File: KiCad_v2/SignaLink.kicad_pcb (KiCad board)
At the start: 2 copper layers, 60.2 x 45 mm, 74 parts, among them U1 MT3608, U2 ESP32-C3_SUPERMINI_TH, U3 DM-OLED096-636, U4 MPU-6050, U5 BNO085, U6 MCP73871, U7 LTC4415IMSE_PBF, U8 TPS54331

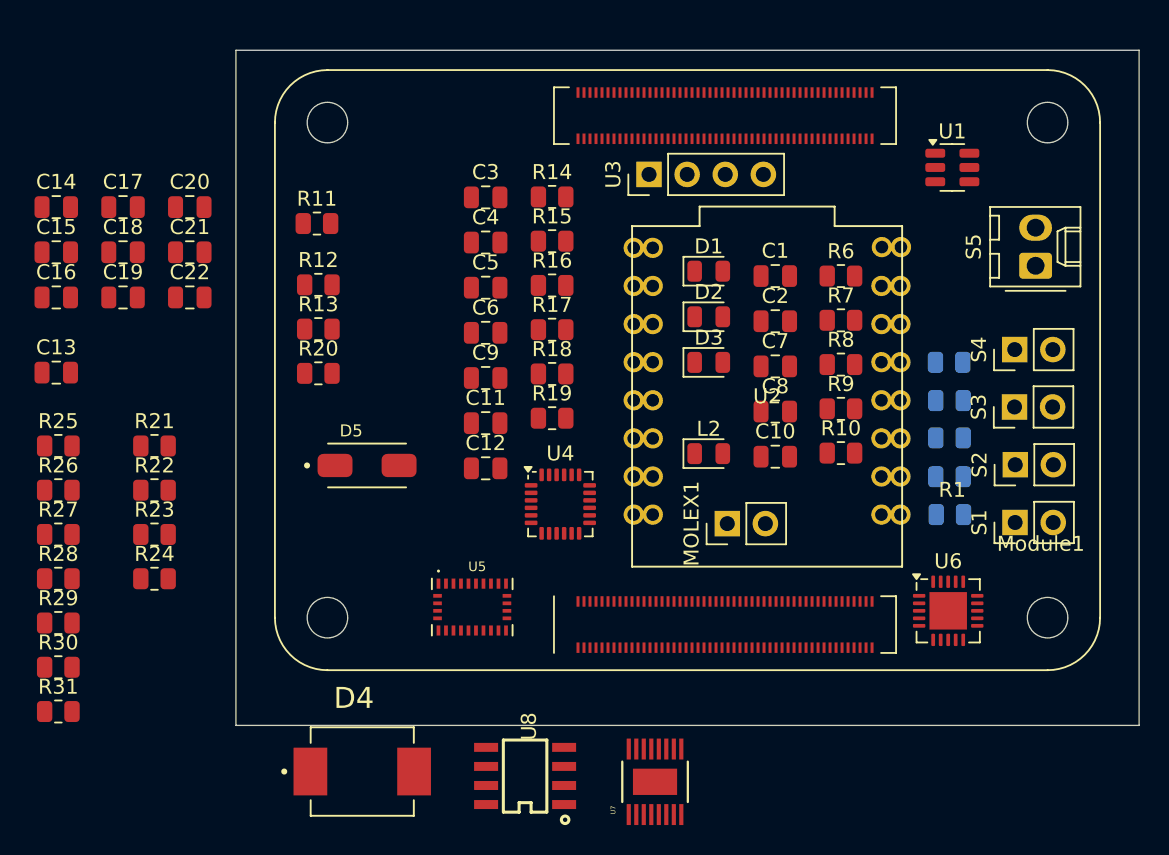
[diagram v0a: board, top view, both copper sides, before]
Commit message: feat: agrego 3d de ESP32 Y CM4
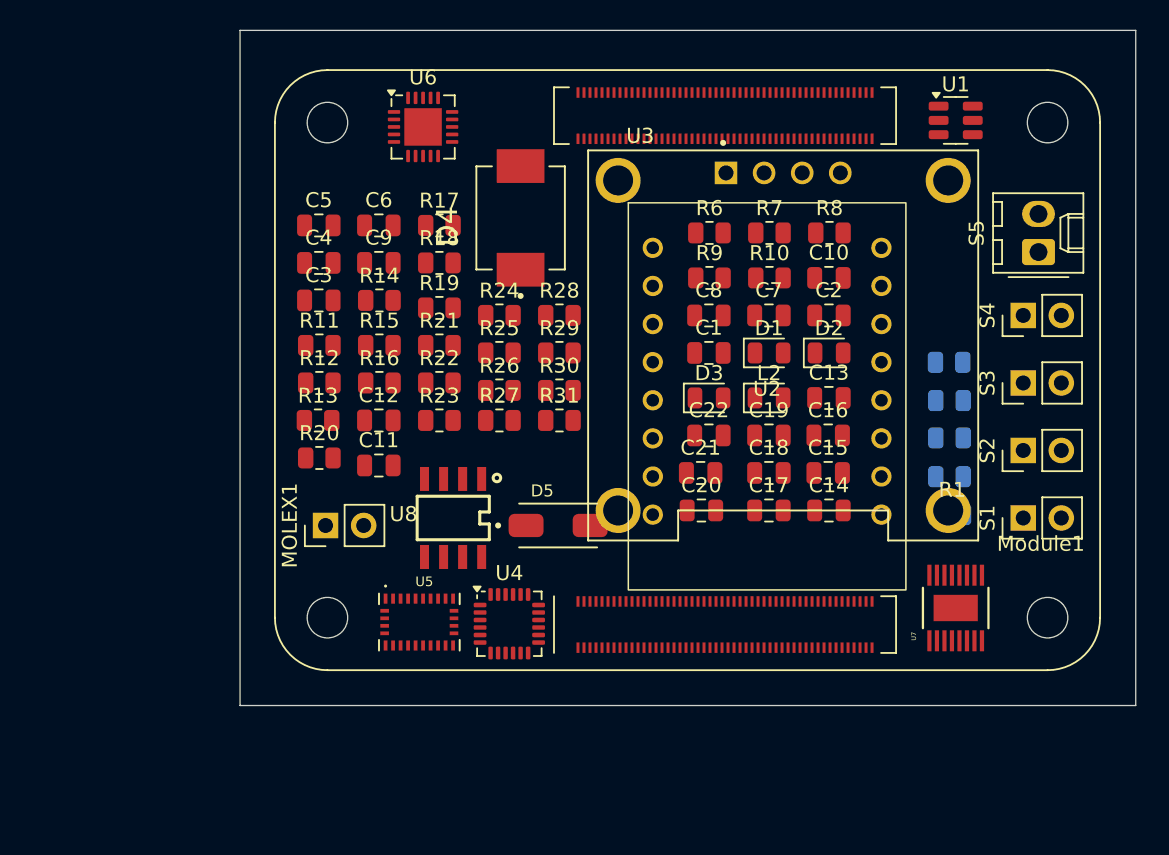
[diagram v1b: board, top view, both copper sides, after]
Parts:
- D4: footprint Footprint KiCad:DIOM7959X265N -> Custom_Footprints:DIOM7959X265N
- D5: footprint Footprint KiCad:B340A -> Custom_Footprints:B340A
- L2: value 22uH-4.7u -> 4.7uH
- U2: footprint esp32-huella:MODULE_ESP32-C3_SUPERMINI_TH -> Custom_Footprints:MODULE_ESP32-C3_SUPERMINI_TH
- U3: footprint Connector_PinHeader_2.54mm:PinHeader_1x04_P2.54mm_Vertical -> Custom_Footprints:MODULE_DM-OLED096-636
- U5: footprint Footprint KiCad:IC_BNO085 -> Custom_Footprints:IC_BNO085
- U7: footprint Footprint KiCad:MSOP-16_MSE -> Custom_Footprints:MSOP-16_MSE
- U8: footprint Footprint KiCad:SOP8 -> Custom_Footprints:SOP8
- moved C14 55.3 mm to (73.0, 79.0)
- moved C15 53.5 mm to (73.0, 76.5)
- moved C16 52.3 mm to (73.0, 74.0)
- moved C13 51.5 mm to (73.0, 71.5)
- moved U6 47.6 mm to (46.0, 53.4)
- moved C17 47.6 mm to (69.0, 79.0)
- moved C18 45.5 mm to (69.0, 76.5)
- moved C19 44.0 mm to (69.0, 74.0)
- moved C20 39.6 mm to (64.5, 79.0)
- moved R31 38.6 mm to (55.1, 73.0)
- moved D4 38.4 mm to (52.5, 59.5), turned to 90 degrees
- moved R30 38.2 mm to (55.1, 71.0)
- moved R29 37.9 mm to (55.1, 68.5)
- moved R28 37.7 mm to (55.1, 66.0)
- moved C21 37.1 mm to (64.5, 76.5)
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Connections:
- U2 pad 0: /A0 -> unconnected-(U2-GPIO0-Pad0)
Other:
- board size 60.2 x 45 mm -> 59.7 x 45 mm

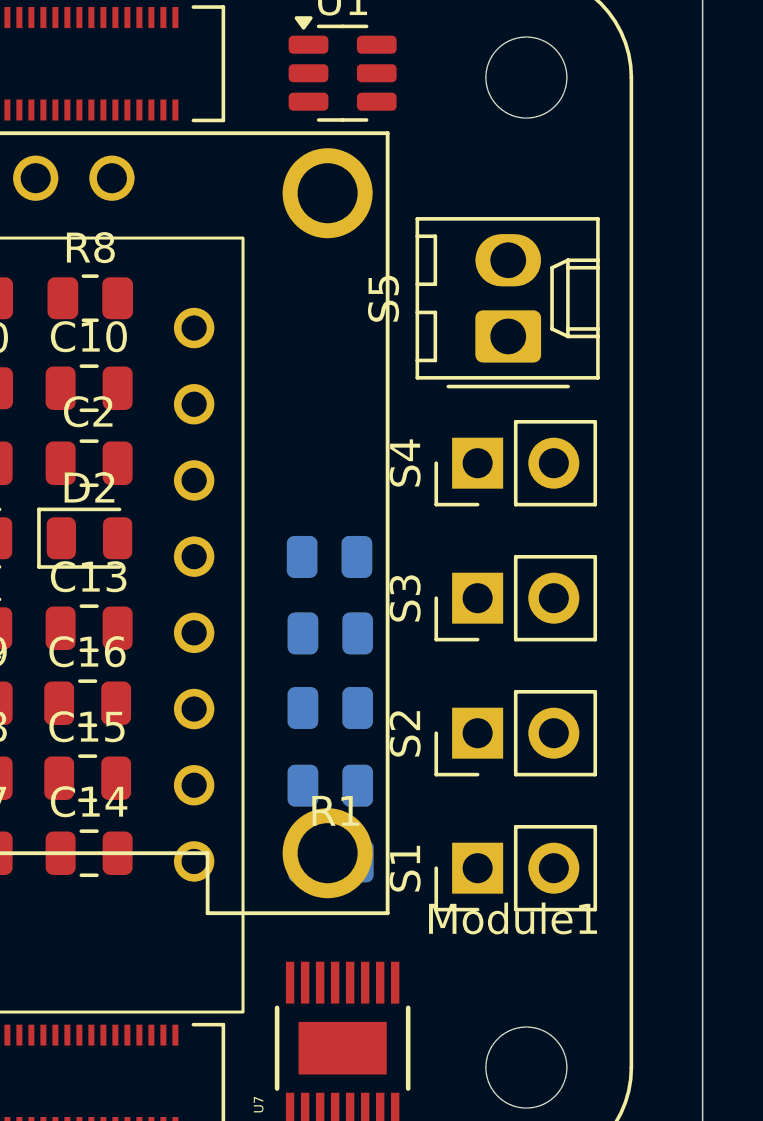
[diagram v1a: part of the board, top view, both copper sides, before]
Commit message: feat:footprint de molex en flex
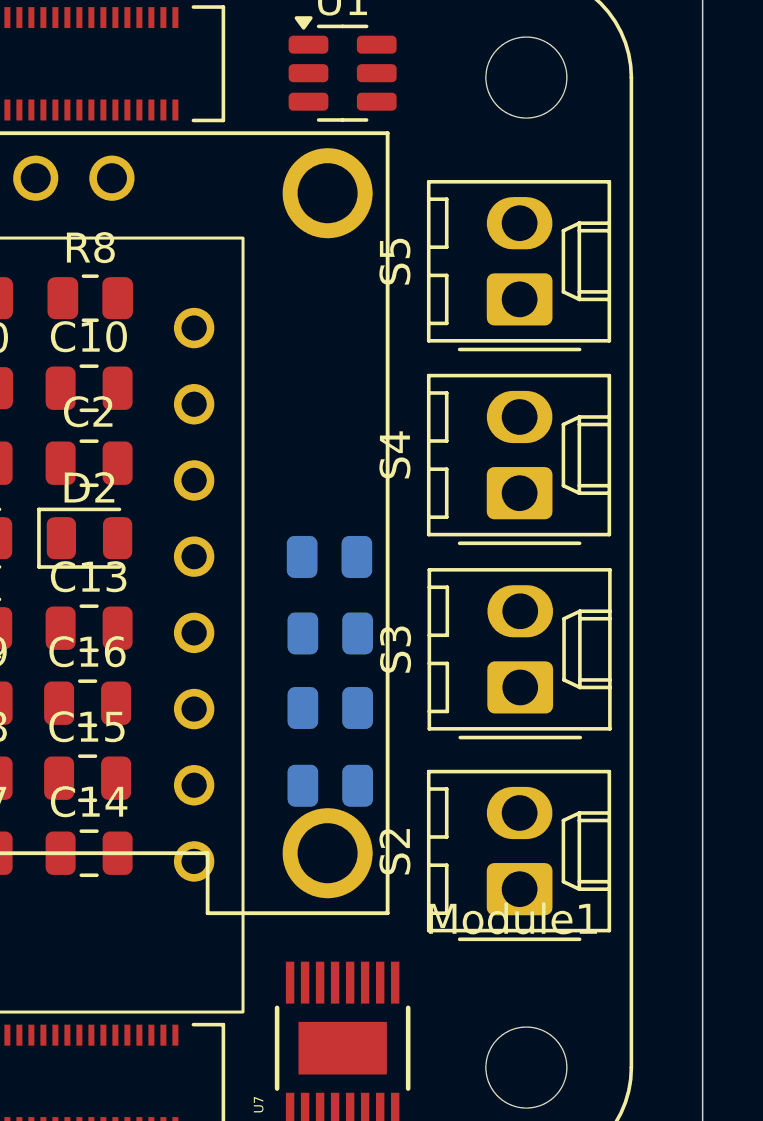
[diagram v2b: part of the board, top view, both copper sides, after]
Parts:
- removed R1: 10k, Resistor_SMD:R_0805_2012Metric
- removed S1: SF 1, Connector_PinHeader_2.54mm:PinHeader_1x02_P2.54mm_Vertical
- S2, S3, S4: footprint Connector_PinHeader_2.54mm:PinHeader_1x02_P2.54mm_Vertical -> Connector_Molex:Molex_KK-254_AE-6410-02A_1x02_P2.54mm_Vertical
- moved S2 5.39 mm to (87.4, 80.2)
- moved S3 3.30 mm to (87.4, 73.5)
- moved S4 1.72 mm to (87.4, 67.0)
- moved S5 1.29 mm to (87.4, 60.5)

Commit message: chore: pocos cambios
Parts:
- moved U2 0.90 mm to (69.4, 70.6)
- moved Module1 0.40 mm to (88.0, 86.0)
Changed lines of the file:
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@@
 	(footprint "CM4IO:Raspberry-Pi-4-Compute-Module"
 		(layer "F.Cu")
-		(at 87.625 86.145 90)
+		(at 88 86 90)
 		(descr "Raspberry Pi 4 Compute Module")
 		(tags "Raspberry Pi 4 Compute Module")
@@
 		)
 		(embedded_fonts no)
-		(model "${KICAD_3DMODELS}/CM4.step"
+		(model "${KIPRJMOD}/libs/3dmodels/CM4.step"
 			(offset
-				(xyz 52.4 51.5 -2.8)
+				(xyz -19.3 -3 -2.8)
 			)
 			(scale
@@
 			)
 			(rotate
-				(xyz -0 -180 -90)
+				(xyz -180 -0 -90)
 			)
 		)
@@
 	(footprint "Custom_Footprints:MODULE_ESP32-C3_SUPERMINI_TH"
 		(layer "F.Cu")
-		(at 68.93 71.395)
+		(at 69.38 70.62)
 		(property "Reference" "U2"
 			(at 0 -0.5 0)
@@
 		)
 		(embedded_fonts no)
-		(model "${KICAD_3DMODELS}/ESP32-C3_SUPERMINI_TH.step"
+		(model "${KIPRJMOD}/libs/3dmodels/ESP32-C3_SUPERMINI_TH.step"
 			(offset
 				(xyz 0 0 0)

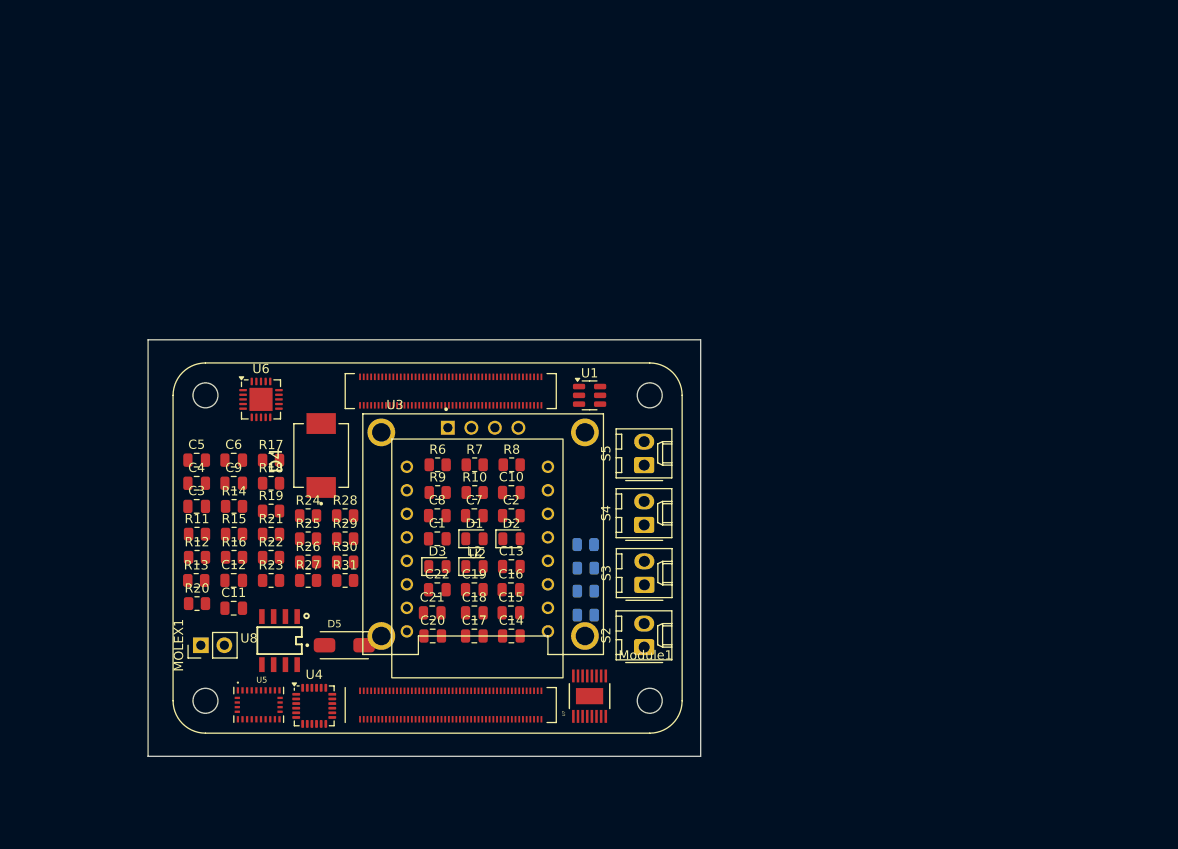
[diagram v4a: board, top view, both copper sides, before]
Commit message: agrego step up para 3A con su debido esquematico
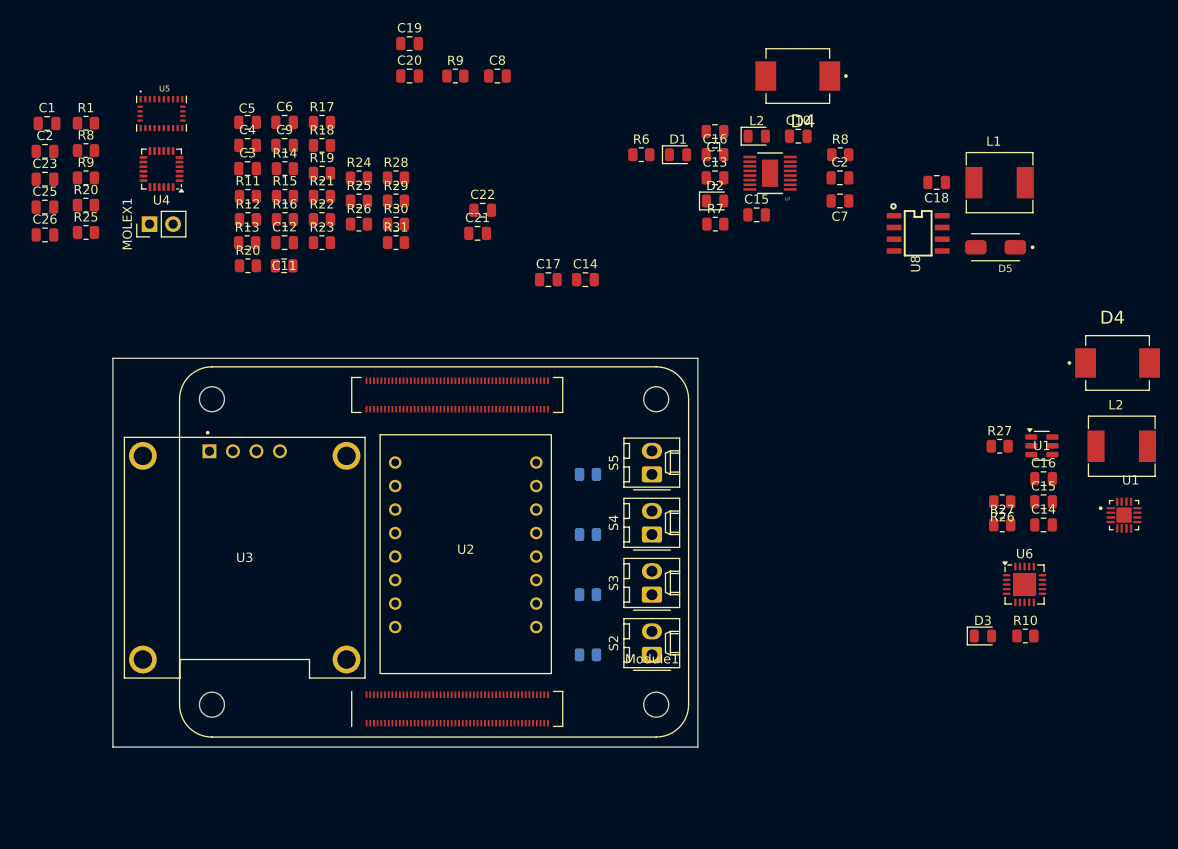
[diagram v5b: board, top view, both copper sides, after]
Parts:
- added C1: 22uF, Capacitor_SMD:C_0805_2012Metric, F.Cu at (22.9, 23.6)
- added C14: 0.01uF, Capacitor_SMD:C_0805_2012Metric, F.Cu at (130.6, 67.0)
- added C15: 0.01uF, Capacitor_SMD:C_0805_2012Metric, F.Cu at (130.6, 64.5)
- added C16: 0.01uF, Capacitor_SMD:C_0805_2012Metric, F.Cu at (130.6, 62.0)
- added C2: 47uF, Capacitor_SMD:C_0805_2012Metric, F.Cu at (22.7, 26.6)
- added C23: 10nF, Capacitor_SMD:C_0805_2012Metric, F.Cu at (22.7, 29.6)
- added C25: 4.7nf, Capacitor_SMD:C_0805_2012Metric, F.Cu at (22.7, 32.7)
- added C26: 47uF, Capacitor_SMD:C_0805_2012Metric, F.Cu at (22.7, 35.7)
- added D4: SS34, Custom_Footprints:DIOM7959X265N, F.Cu at (138.5, 49.5)
- added L1: 6.8uF, Custom_Footprints:IND_SRP6540-100M, F.Cu at (125.8, 30.0)
- added L2: 6.8uH, Custom_Footprints:IND_SRP6540-100M, F.Cu at (139.0, 58.5)
- added R1: 153k, Resistor_SMD:R_0805_2012Metric, F.Cu at (27.1, 23.6)
- added R20: 33k, Resistor_SMD:R_0805_2012Metric, F.Cu at (27.1, 32.5)
- added R25: 100k, Resistor_SMD:R_0805_2012Metric, F.Cu at (27.1, 35.4)
- added R26: 332k, Resistor_SMD:R_0805_2012Metric, F.Cu at (126.1, 64.5)
- added R27: 68.1, Resistor_SMD:R_0805_2012Metric, F.Cu at (125.8, 58.5)
- added R8: 49.9k, Resistor_SMD:R_0805_2012Metric, F.Cu at (27.1, 26.6)
- added R9: 78.7k, Resistor_SMD:R_0805_2012Metric, F.Cu at (27.1, 29.5)
- added U1: TPS55340RTER, Custom_Footprints:QFN50P300X300X80-17N, F.Cu at (139.2, 65.9)
- R12: value 2k2 -> 1k
- R13: value R -> 22k
- R22, R23: value 124 -> 1.58k
- moved U6 84.9 mm to (128.5, 73.4)
- moved D5 82.5 mm to (125.4, 37.0), turned to 180 degrees
- moved U8 81.8 mm to (117.0, 35.5), turned to -90 degrees
- moved R27 75.2 mm to (126.1, 67.0)
- moved C18 68.2 mm to (119.0, 30.0), turned to 180 degrees
- moved D4 65.8 mm to (104.0, 18.5), turned to 180 degrees
- moved U5 64.7 mm to (35.2, 22.6)
- moved R10 61.5 mm to (128.6, 79.0)
- moved C20 60.6 mm to (62.0, 18.5)
- moved U4 60.3 mm to (35.2, 28.6), turned to 180 degrees
- moved U7 59.8 mm to (101.0, 29.0), turned to 180 degrees
- moved C19 59.4 mm to (62.0, 15.0)
- moved D3 59.4 mm to (124.0, 79.0)
- moved L2 55.6 mm to (99.6, 25.0)
- moved C1 53.3 mm to (95.0, 24.5), turned to 180 degrees
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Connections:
- C8 pad 1: GND -> /IN1
- C8 pad 2: /IN1 -> GND
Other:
- board size 59.7 x 45 mm -> 63.2 x 42 mm

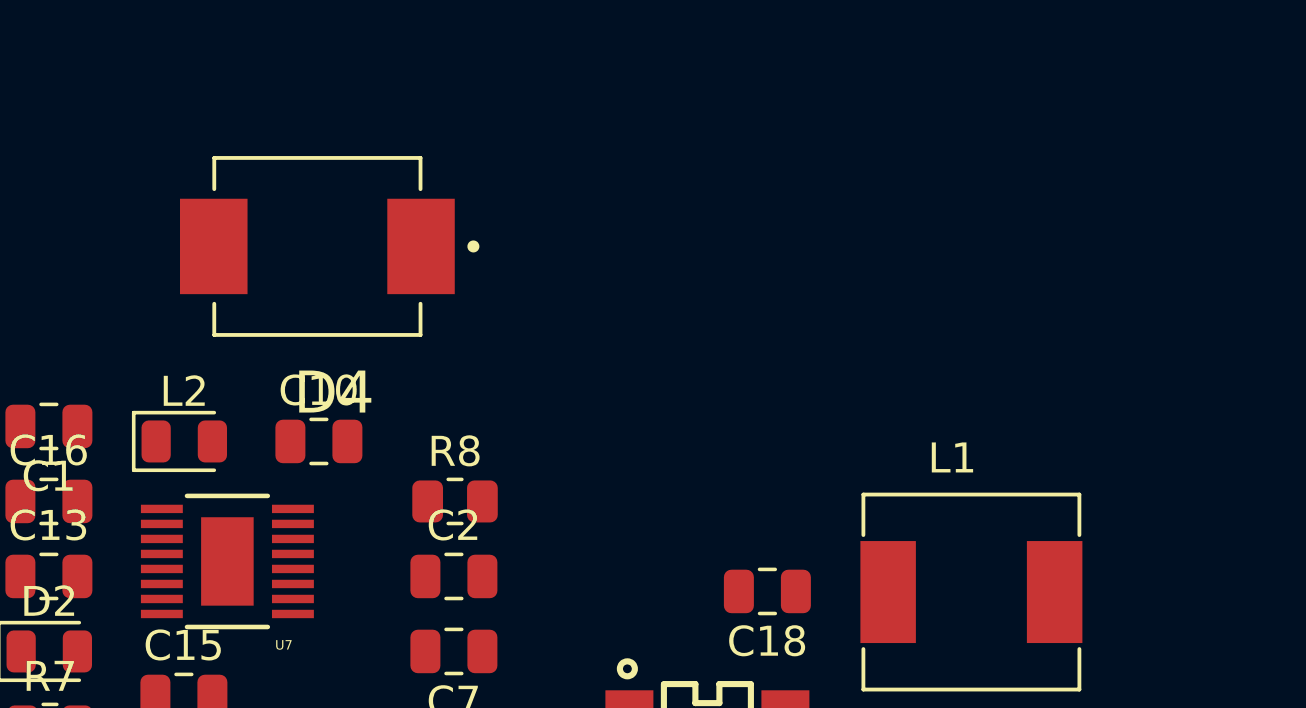
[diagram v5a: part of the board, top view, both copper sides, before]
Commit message: agrego boton de wake
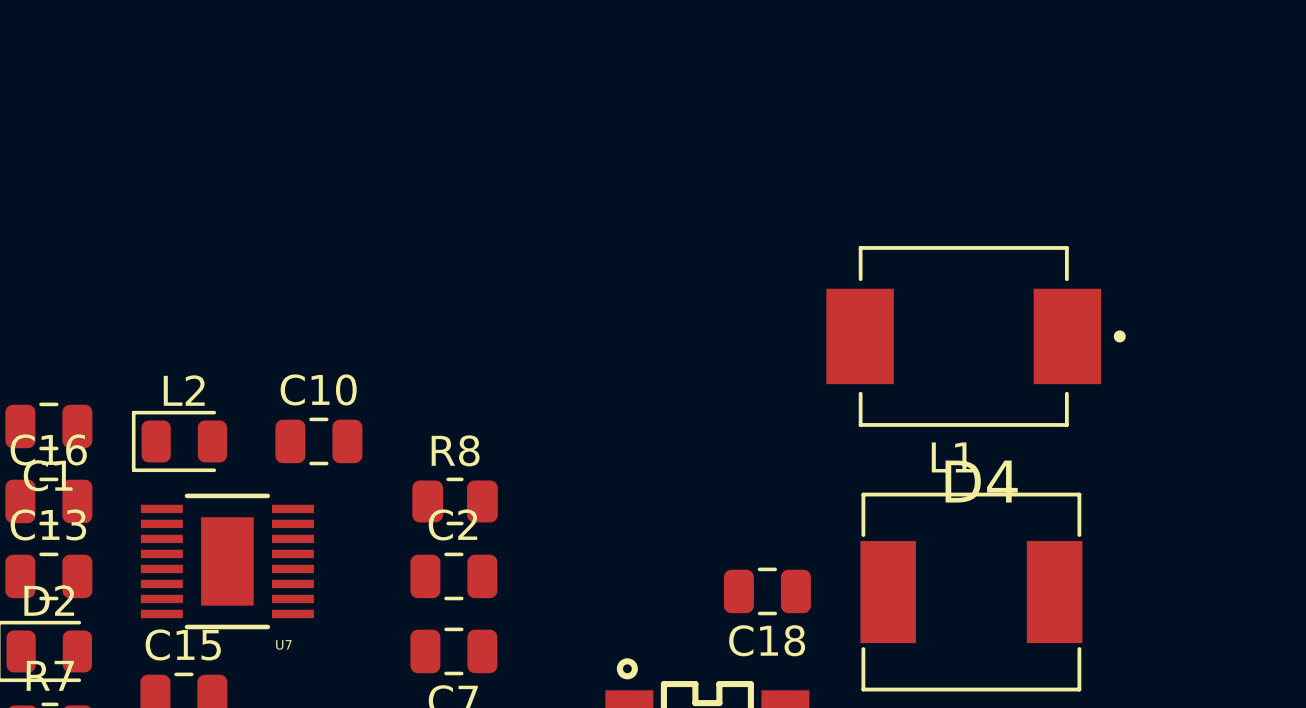
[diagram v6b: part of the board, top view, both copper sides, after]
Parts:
- moved D4 21.8 mm to (125.5, 21.5)
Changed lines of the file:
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@@
 	(footprint "Custom_Footprints:DIOM7959X265N"
 		(layer "F.Cu")
-		(at 104 18.5 180)
+		(at 125.545 21.5 180)
 		(property "Reference" "D4"
 			(at -0.555 -4.889 0)
